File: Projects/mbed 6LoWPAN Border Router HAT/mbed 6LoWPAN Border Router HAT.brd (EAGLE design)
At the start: 65 x 56.5 mm, 83 parts, among them CON1 TC2030-CTX-NL, CON2 USB_MICROB, IC1 CAT24C32WI-GT3, IC2 74LVC1GXX, IC3 MK64FN1M0VLL12, IC4 LPC11U35FHI33/501, IC5 USBLC6-2SC6, IC6 LD1117S33, Q1 32.768kHz, Q2 12MHz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

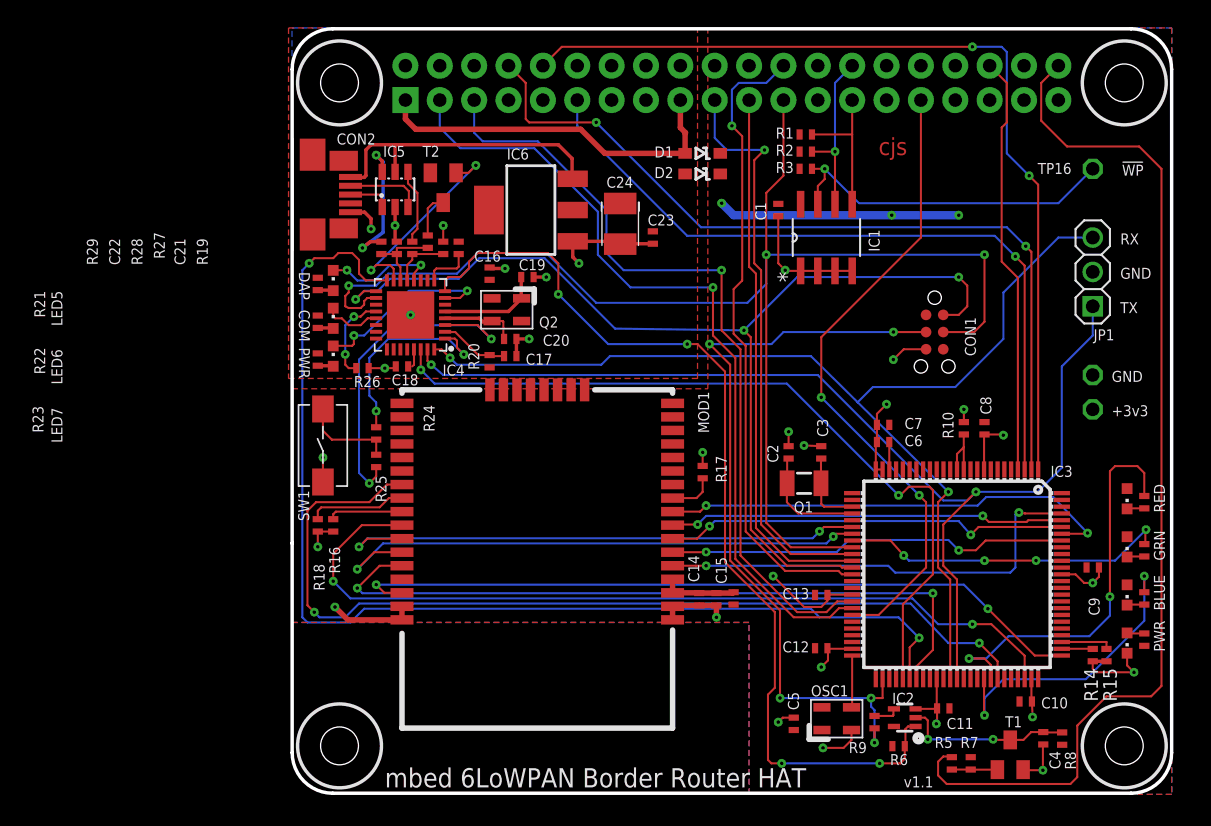
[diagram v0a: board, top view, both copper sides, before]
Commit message: Updated 6LoWPAN Border Router HDK to Rev 1.1
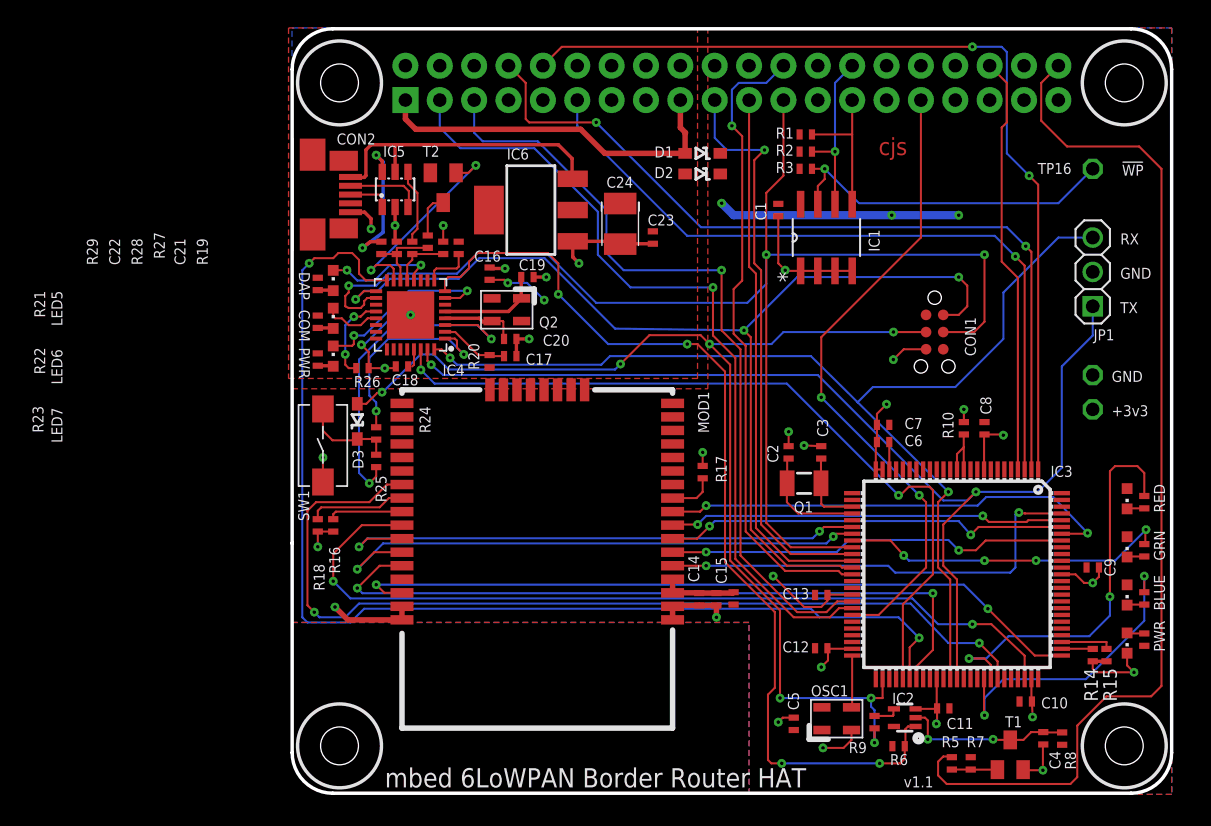
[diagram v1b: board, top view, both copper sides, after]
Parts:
- added D3: BAT60J, mbed-HDK:BAT60A
- R9: value 10k -> 1k
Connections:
- net N$5: now also D3.K
- net TGT_NRESET: now also D3.A
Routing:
- net TGT_NRESET: track 58.1 -> 87.5 mm, vias 5 -> 7
- net GND: track 98.9 -> 105.6 mm, vias 30 -> 31
- net +3.3V_IF: track 1.31 -> 6.17 mm, vias 0 -> 2
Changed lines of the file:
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@@
 <?xml version="1.0" encoding="utf-8"?>
 <!DOCTYPE eagle SYSTEM "eagle.dtd">
-<eagle version="7.3.0">
+<eagle version="7.6.0">
 <drawing>
 <settings>
@@
 <setting verticaltext="up"/>
 </settings>
-<grid distance="0.005" unitdist="inch" unit="inch" style="dots" multiple="1" display="yes" altdistance="0.025" altunitdist="inch" altunit="inch"/>
+<grid distance="2" unitdist="mil" unit="mil" style="dots" multiple="1" display="no" altdistance="0.025" altunitdist="inch" altunit="mil"/>
 <layers>
 <layer number="1" name="Top" color="4" fill="1" visible="yes" active="yes"/>
@@
 </element>
 <element name="C9" library="mbed-HDK" package="0402" value="100nF" x="50.8" y="-34.544" locked="yes" smashed="yes">
-<attribute name="NAME" x="51.308" y="-38.1" size="0.8128" layer="25" font="vector" ratio="12" rot="R90"/>
+<attribute name="NAME" x="52.4764" y="-35.2044" size="0.8128" layer="25" font="vector" ratio="12" rot="R90"/>
 <attribute name="VALUE" x="50.165" y="-36.449" size="1.27" layer="27"/>
 </element>
@@
 </element>
 <element name="R5" library="mbed-HDK" package="0402" value="220R" x="40.386" y="-49.022" locked="yes" smashed="yes" rot="R90">
-<attribute name="NAME" x="39.116" y="-47.879" size="0.8128" layer="25" font="vector" ratio="12"/>
+<attribute name="NAME" x="39.624" y="-47.8282" size="0.8128" layer="25" font="vector" ratio="12"/>
 <attribute name="VALUE" x="42.291" y="-49.657" size="1.27" layer="27" rot="R90"/>
 </element>
 <element name="R7" library="mbed-HDK" package="0402" value="10k" x="41.783" y="-49.022" locked="yes" smashed="yes" rot="R270">
-<attribute name="NAME" x="41.021" y="-47.879" size="0.8128" layer="25" font="vector" ratio="12"/>
+<attribute name="NAME" x="41.4782" y="-47.8282" size="0.8128" layer="25" font="vector" ratio="12"/>
 <attribute name="VALUE" x="39.878" y="-48.387" size="1.27" layer="27" rot="R270"/>
 </element>
@@
 </element>
 <element name="R24" library="mbed-HDK" package="0402" value="33R" x="-2.159" y="-24.638" locked="yes" smashed="yes" rot="R270">
-<attribute name="NAME" x="2.159" y="-24.511" size="0.8128" layer="21" font="vector" ratio="12" rot="R90"/>
+<attribute name="NAME" x="1.8542" y="-24.6126" size="0.8128" layer="21" font="vector" ratio="12" rot="R90"/>
 </element>
 <element name="R25" library="mbed-HDK" package="0402" value="33R" x="-2.159" y="-26.67" locked="yes" smashed="yes" rot="R90">
@@
 <attribute name="VALUE" x="35.179" y="-51.562" size="1.016" layer="27" font="vector" ratio="12"/>
 </element>
-<element name="R9" library="mbed-HDK" package="0402" value="10k" x="34.671" y="-45.974" smashed="yes" rot="R90">
+<element name="R9" library="mbed-HDK" package="0402" value="1k" x="34.671" y="-45.974" smashed="yes" rot="R90">
 <attribute name="NAME" x="32.766" y="-48.26" size="0.8128" layer="25" font="vector" ratio="12"/>
 <attribute name="VALUE" x="38.481" y="-47.244" size="1.016" layer="27" font="vector" ratio="12" rot="R90"/>
+</element>
+<element name="D3" library="mbed-HDK" package="BAT60A" value="BAT60J" x="-3.556" y="-23.749" smashed="yes" rot="R90">
+<attribute name="NAME" x="-3.0988" y="-27.2542" size="0.8128" layer="25" font="vector" ratio="12" rot="R90"/>
+<attribute name="VALUE" x="-1.016" y="-26.289" size="1.016" layer="27" font="vector" ratio="12" rot="R90"/>
 </element>
 </elements>
@@
 <wire x1="33.017" y1="-40.552" x2="31.2302" y2="-40.552" width="0.1524" layer="1"/>
 <wire x1="31.2302" y1="-40.552" x2="31.1912" y2="-40.513" width="0.1524" layer="1"/>
-<wire x1="31.2942" y1="-36.552" x2="33.017" y2="-36.552" width="0.1524" layer="1"/>
+<wire x1="31.2152" y1="-36.552" x2="33.017" y2="-36.552" width="0.1524" layer="1"/>
 <via x="28.321" y="-24.511" extent="1-16" drill="0.254"/>
 <wire x1="35.267" y1="-27.302" x2="34.767" y2="-27.302" width="0.1524" layer="1"/>
@@
 <wire x1="32.385" y1="-47.879" x2="32.9692" y2="-47.2948" width="0.1524" layer="1"/>
 <wire x1="32.9692" y1="-47.2948" x2="32.9692" y2="-46.5582" width="0.1524" layer="1"/>
-<wire x1="15.875" y1="-10.671" x2="15.875" y2="-10.644" width="0" layer="19" extent="1-1"/>
-<wire x1="31.2942" y1="-36.552" x2="31.242" y2="-36.5252" width="0" layer="19" extent="1-1"/>
+<wire x1="0.381" y1="-15.875" x2="0.3556" y2="-15.9004" width="0.1524" layer="16"/>
+<wire x1="0.3556" y1="-15.9004" x2="-0.8636" y2="-15.9004" width="0.1524" layer="16"/>
+<wire x1="-0.8636" y1="-15.9004" x2="-3.048" y2="-18.0848" width="0.1524" layer="16"/>
+<wire x1="-3.048" y1="-18.0848" x2="-3.2512" y2="-18.0848" width="0.1524" layer="16"/>
+<via x="-3.2512" y="-18.0848" extent="1-16" drill="0.254"/>
+<wire x1="-2.7178" y1="-19.812" x2="-2.7178" y2="-18.6182" width="0.1524" layer="1"/>
+<wire x1="-2.7178" y1="-18.6182" x2="-3.2512" y2="-18.0848" width="0.1524" layer="1"/>
+<wire x1="15.875" y1="-10.671" x2="15.875" y2="-10.644" width="0.1524" layer="1"/>
+<wire x1="31.2152" y1="-36.552" x2="31.1912" y2="-36.576" width="0.1524" layer="1"/>
 </signal>
 <signal name="+3.3V">
@@
 <wire x1="0.635" y1="-19.558" x2="0.635" y2="-18.429" width="0.1524" layer="1"/>
 <wire x1="0.635" y1="-18.429" x2="0.631" y2="-18.425" width="0.1524" layer="1"/>
-<wire x1="6.223" y1="-13.2842" x2="3.937" y2="-10.4648" width="0" layer="19" extent="1-1"/>
+<wire x1="6.223" y1="-13.2842" x2="7.3406" y2="-13.2842" width="0.1524" layer="1"/>
+<wire x1="7.3406" y1="-13.2842" x2="7.5692" y2="-13.5128" width="0.1524" layer="1"/>
+<via x="7.5692" y="-13.5128" extent="1-16" drill="0.254"/>
+<wire x1="7.5692" y1="-13.5128" x2="8.9916" y2="-13.5128" width="0.1524" layer="16"/>
+<wire x1="8.9916" y1="-13.5128" x2="10.2616" y2="-14.7828" width="0.1524" layer="16"/>
+<via x="10.2616" y="-14.7828" extent="1-16" drill="0.254"/>
+<wire x1="10.2616" y1="-14.7828" x2="10.3124" y2="-14.7828" width="0.1524" layer="1"/>
+<wire x1="10.3124" y1="-14.7828" x2="10.414" y2="-14.8844" width="0.1524" layer="1"/>
 </signal>
 <signal name="USB-DP">
@@
 <wire x1="34.671" y1="-45.085" x2="34.417" y2="-44.831" width="0.1524" layer="16"/>
 <wire x1="34.417" y1="-44.831" x2="34.417" y2="-44.196" width="0.1524" layer="16"/>
+<contactref element="D3" pad="A"/>
+<wire x1="-3.556" y1="-22.449" x2="-2.891" y2="-22.449" width="0.1524" layer="1"/>
+<wire x1="-2.891" y1="-22.449" x2="-2.0828" y2="-21.6408" width="0.1524" layer="1"/>
+<wire x1="-2.0828" y1="-21.6408" x2="-1.778" y2="-21.6408" width="0.1524" layer="1"/>
+<wire x1="-1.778" y1="-21.6408" x2="-1.7272" y2="-21.59" width="0.1524" layer="1"/>
+<via x="-1.7272" y="-21.59" extent="1-16" drill="0.254"/>
+<wire x1="-1.7272" y1="-21.59" x2="-1.6764" y2="-21.59" width="0.1524" layer="16"/>
+<wire x1="-1.6764" y1="-21.59" x2="1.1176" y2="-18.796" width="0.1524" layer="16"/>
+<wire x1="1.1176" y1="-18.796" x2="2.0828" y2="-18.796" width="0.1524" layer="16"/>
+<wire x1="2.0828" y1="-18.796" x2="3.2004" y2="-19.9136" width="0.1524" layer="16"/>
+<wire x1="3.2004" y1="-19.9136" x2="15.494" y2="-19.9136" width="0.1524" layer="16"/>
+<wire x1="15.494" y1="-19.9136" x2="15.9004" y2="-19.5072" width="0.1524" layer="16"/>
+<via x="15.9004" y="-19.5072" extent="1-16" drill="0.254"/>
+<wire x1="15.9004" y1="-19.5072" x2="18.034" y2="-17.3736" width="0.1524" layer="1"/>
+<wire x1="18.034" y1="-17.3736" x2="21.8186" y2="-17.3736" width="0.1524" layer="1"/>
+<wire x1="21.8186" y1="-17.3736" x2="22.479" y2="-18.034" width="0.1524" layer="1"/>
 </signal>
 <signal name="N$1">
@@
 <contactref element="SW1" pad="P$2"/>
 <wire x1="-2.159" y1="-26.2128" x2="-2.159" y2="-25.0952" width="0.1524" layer="1"/>
-<wire x1="-2.159" y1="-25.0952" x2="-5.4356" y2="-25.0952" width="0.1524" layer="1"/>
-<wire x1="-5.4356" y1="-25.0952" x2="-6.096" y2="-24.4348" width="0.1524" layer="1"/>
-<wire x1="-6.096" y1="-24.4348" x2="-6.096" y2="-22.827" width="0.1524" layer="1"/>
+<contactref element="D3" pad="K"/>
+<wire x1="-6.096" y1="-22.827" x2="-6.096" y2="-24.4348" width="0.1524" layer="1"/>
+<wire x1="-6.096" y1="-24.4348" x2="-5.3848" y2="-25.146" width="0.1524" layer="1"/>
+<wire x1="-5.3848" y1="-25.146" x2="-3.653" y2="-25.146" width="0.1524" layer="1"/>
+<wire x1="-3.653" y1="-25.146" x2="-3.556" y2="-25.049" width="0.254" layer="1"/>
+<wire x1="-3.556" y1="-25.049" x2="-2.2052" y2="-25.049" width="0.1524" layer="1"/>
+<wire x1="-2.2052" y1="-25.049" x2="-2.159" y2="-25.0952" width="0.254" layer="1"/>
 </signal>
 <signal name="TGT_NRESET_FB">

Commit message: Rev 1.1 for 6LoWPAN Border Router Hat
Update Gerbers

Cleaned Schematic

Cleaned up silk screen

Updated sch and brd for final build

Added all output CAM files V_1_1

Final version V_1_1 of Border Router Hat Job

Updated ignore files
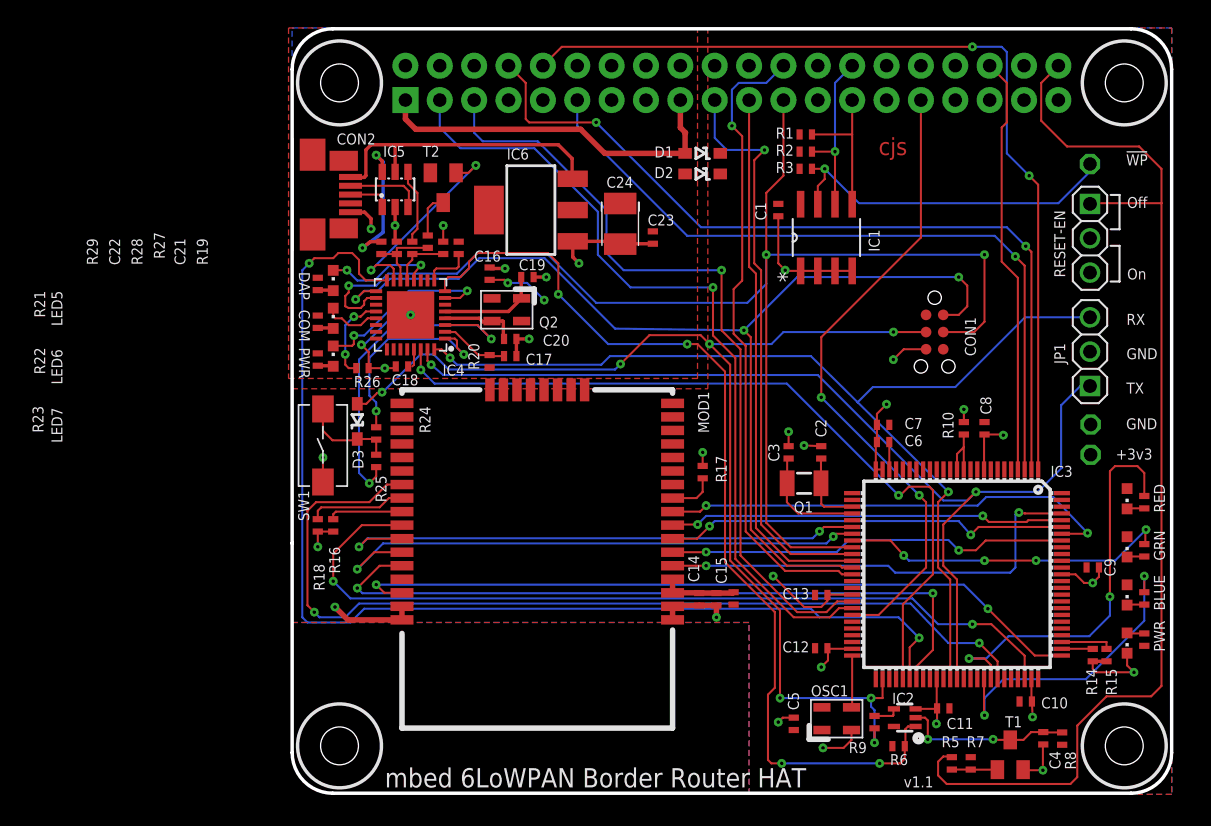
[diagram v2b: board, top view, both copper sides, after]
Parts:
- added RESET-EN: 1X03, mbed-HDK:1X03
- IC2: value 74LVC1GXX -> 74LVC1G08SE-7
- JP1: value DEBUG -> 1X03
- R21: value 470R -> 220R
- moved JP1 5.90 mm to (50.6, -18.6)
- moved TP2 3.66 mm to (50.6, -24.0)
- moved TP1 3.36 mm to (50.6, -26.2)
- moved TP16 0.41 mm to (50.6, -4.72)
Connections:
- net GND: now also RESET-EN.2
- net RPI_K64F_RESET: now also RESET-EN.1
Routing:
- net +3.3V: track 19.8 -> 2.03 mm, vias 3 -> 0
- net K64F_DAPLINK_TX: track 81.1 -> 75.6 mm
- net RPI_K64F_RESET: track 77.4 -> 82.7 mm
- net K64F_DAPLINK_RX: track 81.8 -> 77.2 mm
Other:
- board text added: "Off"
- board text added: "On"
